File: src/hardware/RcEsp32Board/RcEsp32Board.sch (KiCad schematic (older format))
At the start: 2 parts

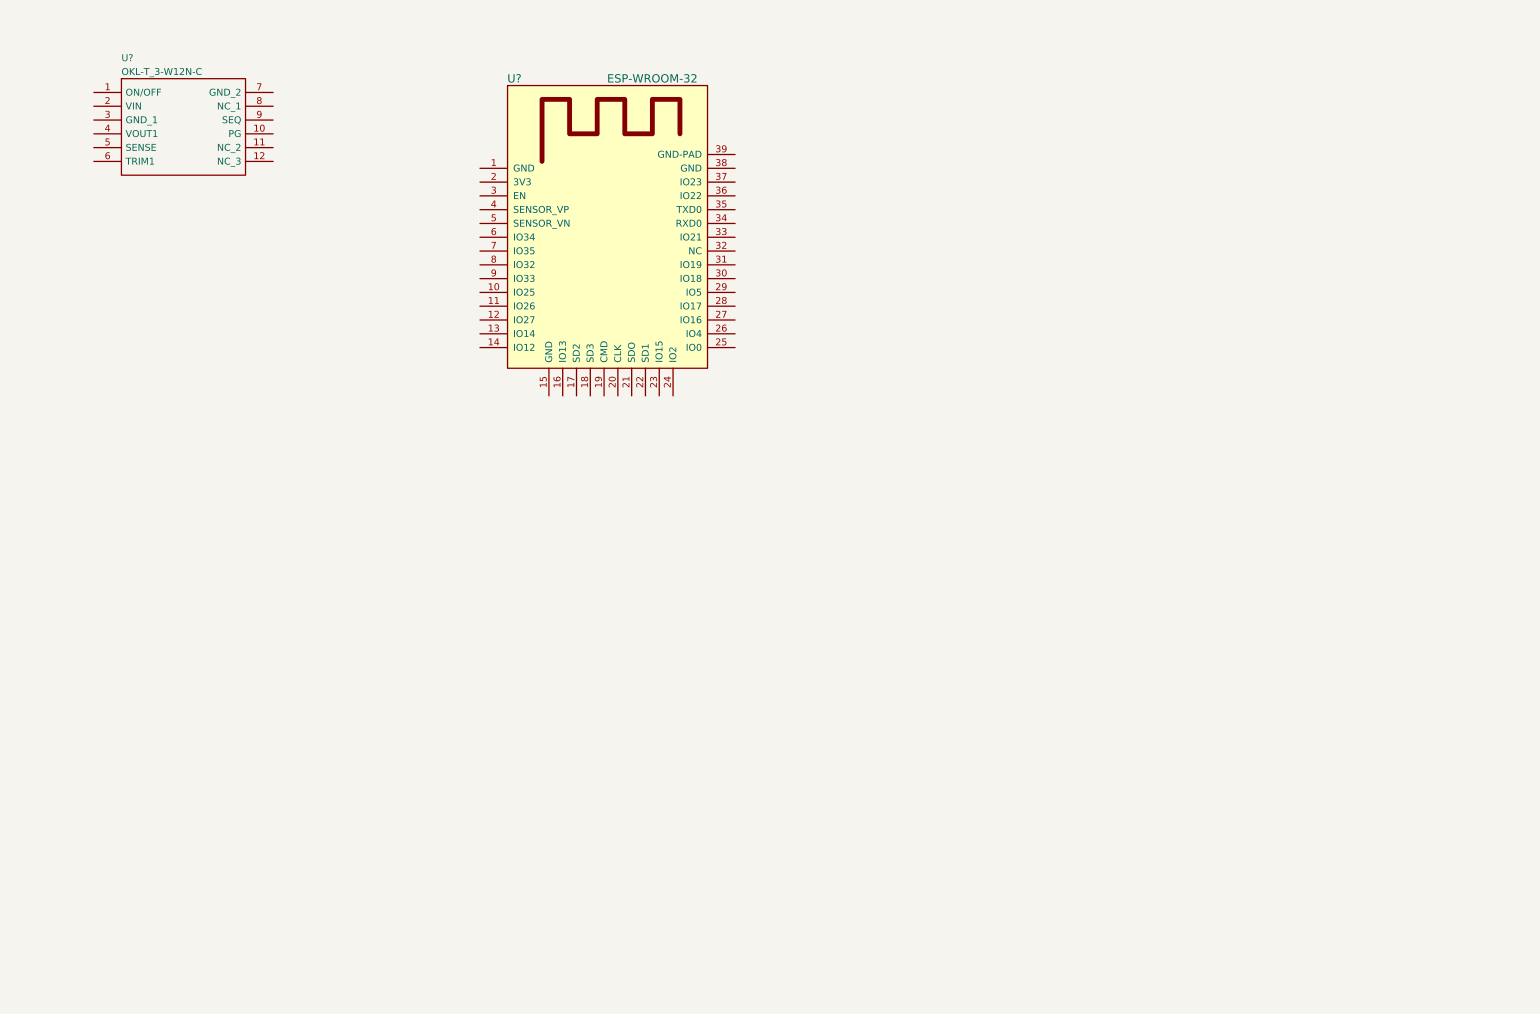
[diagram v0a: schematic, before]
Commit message: add components and update sch
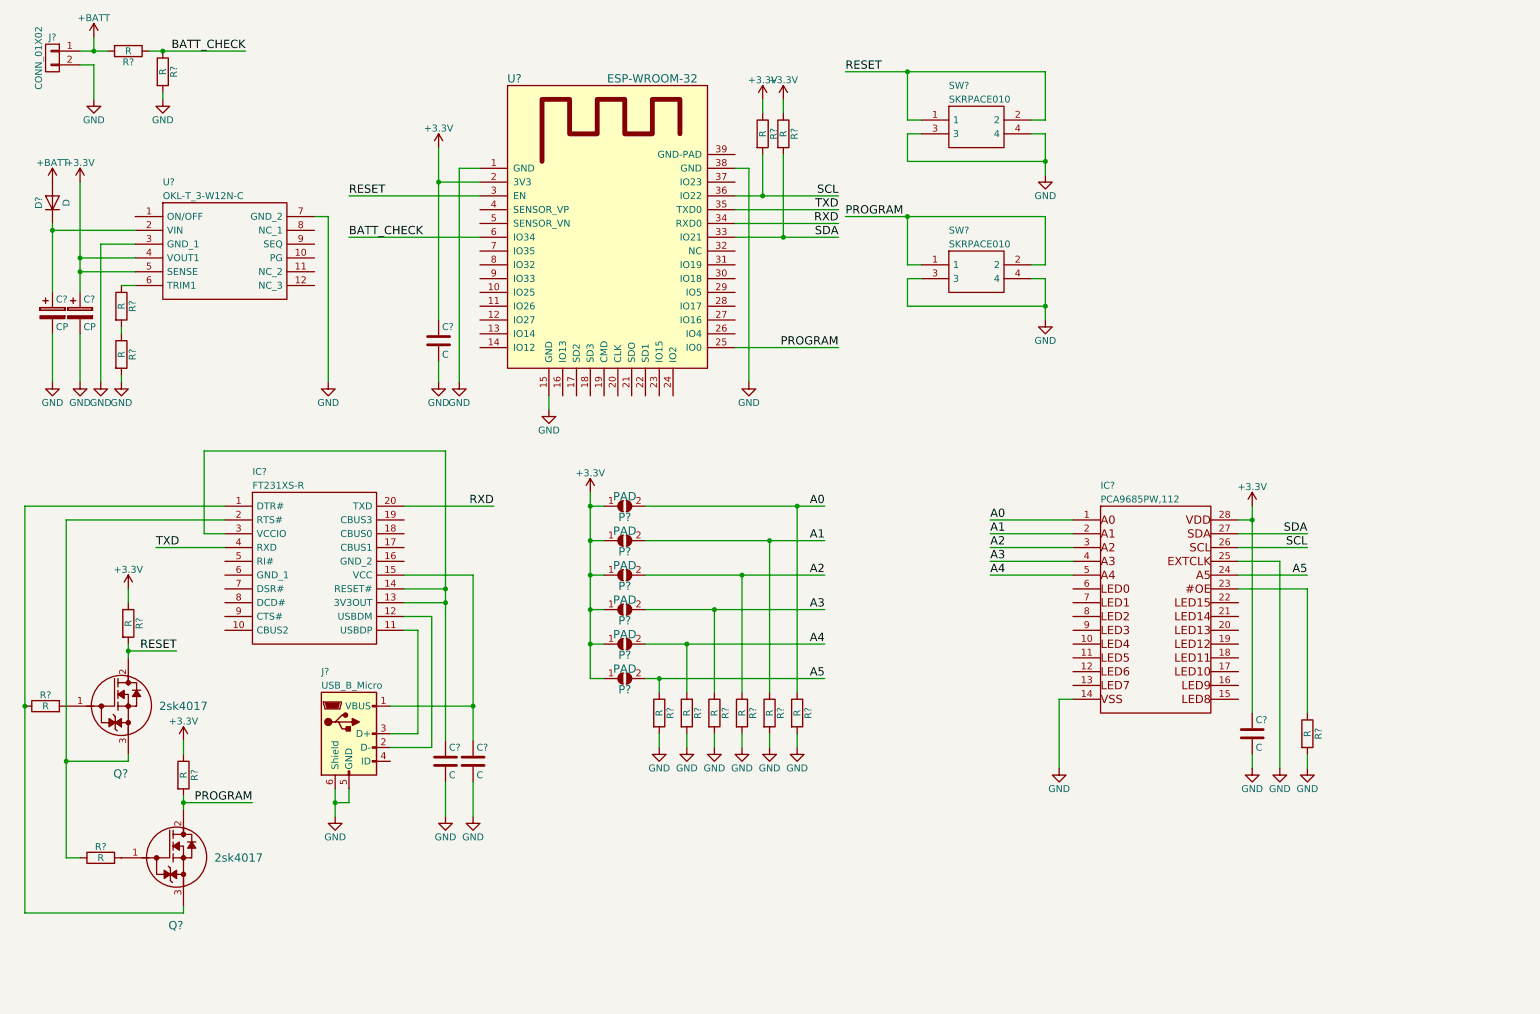
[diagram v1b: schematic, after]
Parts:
- added C? (x2): CP, symbol CP
- added C? (x4): C, symbol C
- added D?: D, symbol D
- added IC?: PCA9685PW,112, Elebot_footprint:SOP65P640X110-28N, symbol PCA9685PW,112
- added IC?: FT231XS-R, Elebot_footprint:SOP64P599X175-20N, symbol FT231XS-R
- added J?: CONN_01X02, Elebot_footprint:PinHeader01x02, symbol CONN_01X02
- added J?: USB_B_Micro, Elebot_footprint:USB_Micro-B_Molex-105133-0001, symbol USB_B_Micro
- added P? (x6): PAD, symbol PAD
- added Q? (x2): 2sk4017, symbol 2sk4017
- added R? (x17): R, symbol R
- added SW? (x2): SKRPACE010, Elebot_footprint:SMT(4.2X3.2), symbol SKRPACE010
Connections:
- net GND: now reaches U?.1 (GND)
- net GND: now also U?.15 (GND), U?.3 (GND_1), U?.38 (GND), U?.7 (GND_2), C?.2, C?.2, C?.2, C?.2, C?.2, C?.2, IC?.14, IC?.25, J?.2 (P2), J?.5 (GND), J?.6 (Shield), R?.2, R?.2, R?.2, R?.2, R?.2, R?.2, R?.2, R?.2, R?.2, SW?.3, SW?.3, SW?.4, SW?.4
- net +3V3: now reaches U?.2 (3V3)
- net +3V3: now also U?.4 (VOUT1), U?.5 (SENSE), C?.1, C?.1, C?.1, IC?.28, P?.1, P?.1, P?.1, P?.1, P?.1, P?.1, R?.1, R?.1, R?.1, R?.1
- net PROGRAM: now reaches U?.25 (IO0)
- net PROGRAM: now also Q?.2, R?.2, SW?.1, SW?.2
- net RESET: now reaches U?.3 (EN)
- net RESET: now also Q?.2, R?.2, SW?.1, SW?.2
- net SDA: now reaches U?.33 (IO21)
- net SDA: now also IC?.27, R?.2
- net RXD: now reaches U?.34 (RXD0)
- net RXD: now also IC?.20 (TXD)
- net TXD: now reaches U?.35 (TXD0)
- net TXD: now also IC?.4 (RXD)
- net SCL: now reaches U?.36 (IO22)
- net SCL: now also IC?.26, R?.2
- net BATT_CHECK: now reaches U?.6 (IO34)
- net BATT_CHECK: now also R?.1, R?.1
- net at U?.2 (VIN): now also C?.1, D?.1 (K)
- net at U?.6 (TRIM1): now also R?.1
- new net: R?.1, R?.2
- new net: IC?.23, R?.1
- new net: IC?.1 (DTR#), Q?.3, R?.1
- new net: IC?.11 (USBDP), J?.3 (D+)
- new net: IC?.12 (USBDM), J?.2 (D-)
- new net: C?.1, IC?.13 (3V3OUT), IC?.14 (RESET#), IC?.3 (VCCIO)
- new net: C?.1, IC?.15 (VCC), J?.1 (VBUS)
- new net: IC?.2 (RTS#), Q?.3, R?.1
- new net: Q?.1, R?.2 (x2)
- new net +BATT: D?.2 (A), J?.1 (P1), R?.2
- new net A0: IC?.1, P?.2, R?.1
- new net A1: IC?.2, P?.2, R?.1
- new net A2: IC?.3, P?.2, R?.1
- new net A3: IC?.4, P?.2, R?.1
- new net A4: IC?.5, P?.2, R?.1
- new net A5: IC?.24, P?.2, R?.1
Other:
- moved on the sheet: U?

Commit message: update
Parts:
- removed C?: C, symbol C
- removed IC?: PCA9685PW,112, Elebot_footprint:SOP65P640X110-28N, symbol PCA9685PW,112
- removed J?: CONN_01X02, Elebot_footprint:PinHeader01x02, symbol CONN_01X02
- removed P? (x6): PAD, symbol PAD
- removed Q? (x2): 2sk4017, symbol 2sk4017
- removed R? (x12): R, symbol R
- added J1: Conn_01x02, FootPrints:EH-2P, symbol Conn_01x02
- added J10, J3, J6, J8: Conn_01x04, FootPrints:PinHeader01x04, symbol Conn_01x04
- added J4, J7, J9: Conn_02x04_Odd_Even, FootPrints:PinHeader02x04, symbol Conn_02x04_Odd_Even
- added J5: Conn_01x03, FootPrints:PinHeader01x03, symbol Conn_01x03
- added LD2: LED, FootPrints:LED_1206_HandSoldering, symbol LED
- added P1, P2: PAD, FootPrints:PAD, symbol PAD
- added R5: 150, FootPrints:R_1206_HandSoldering, symbol R
- added R7, R8: R, FootPrints:R_1206_HandSoldering, symbol R
- C1, C2: renamed from C?; footprint (none) -> FootPrints:elecon_8x10_5
- C3, C4, C5: renamed from C?; value C -> 0.1u; footprint (none) -> FootPrints:C_1206_HandSoldering
- D1: renamed from D?; footprint (none) -> FootPrints:D_SOD-323_HandSoldering
- IC2: renamed from IC?; footprint Elebot_footprint:SOP64P599X175-20N -> FootPrints:SOP64P599X175-20N
- J2: renamed from J?; footprint Elebot_footprint:USB_Micro-B_Molex-105133-0001 -> FootPrints:USB_Micro-B_Molex-105133-0001
- R1: renamed from R?; value R -> 20K; footprint (none) -> FootPrints:R_1206_HandSoldering
- R2, R6: renamed from R?; value R -> 10K; footprint (none) -> FootPrints:R_1206_HandSoldering
- R3: renamed from R?; value R -> 1.5K; footprint (none) -> FootPrints:R_1206_HandSoldering
- R4: renamed from R?; value R -> 680; footprint (none) -> FootPrints:R_1206_HandSoldering
- SW1, SW2: renamed from SW?; footprint Elebot_footprint:SMT(4.2X3.2) -> FootPrints:SMT(4.2X3.2)
- U1: renamed from U?; footprint Elebot_footprint:OKL-T3-W12 -> FootPrints:OKL-T3-W12
- U2: renamed from U?; footprint ESP-WROOM-32 -> FootPrints:ESP-WROOM-32
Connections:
- net +3V3: now also J10.2 (Pin_2), J5.3 (Pin_3), J9.1 (Pin_1), J9.3 (Pin_3), J9.5 (Pin_5), J9.7 (Pin_7), R5.2, R7.1, R8.1
- net +BATT: now also J1.1 (Pin_1), J4.1 (Pin_1), J4.3 (Pin_3), J4.5 (Pin_5), J4.7 (Pin_7), J5.1 (Pin_1)
- net GND: now also U1.1 (ON/OFF), U2.39 (GND-PAD), J1.2 (Pin_2), J10.1 (Pin_1), J4.2 (Pin_2), J4.4 (Pin_4), J4.6 (Pin_6), J4.8 (Pin_8), J7.2 (Pin_2), J7.4 (Pin_4), J7.6 (Pin_6), J7.8 (Pin_8), J9.2 (Pin_2), J9.4 (Pin_4), J9.6 (Pin_6), J9.8 (Pin_8), LD2.1 (K)
- net SCL: now also J10.4 (Pin_4), P1.2
- net SDA: now also J10.3 (Pin_3), P2.2
- net IO0: now reaches U2.10 (IO25)
- net IO0: now also J6.1 (Pin_1)
- net IO1: now reaches U2.11 (IO26)
- net IO1: now also J6.2 (Pin_2)
- net IO2: now reaches U2.12 (IO27)
- net IO2: now also J6.3 (Pin_3)
- net IO3: now reaches U2.13 (IO14)
- net IO3: now also J6.4 (Pin_4)
- net INPUT3: now reaches U2.14 (IO12)
- net INPUT3: now also J8.4 (Pin_4)
- net SVR3: now reaches U2.26 (IO4)
- net SVR3: now also J3.4 (Pin_4)
- net SVR2: now reaches U2.27 (IO16)
- net SVR2: now also J3.3 (Pin_3)
- net SVR1: now reaches U2.28 (IO17)
- net SVR1: now also J3.2 (Pin_2)
- net SVR0: now reaches U2.29 (IO5)
- net SVR0: now also J3.1 (Pin_1)
- net INPUT0: now reaches U2.7 (IO35)
- net INPUT0: now also J8.1 (Pin_1)
- net INPUT1: now reaches U2.8 (IO32)
- net INPUT1: now also J8.2 (Pin_2)
- net INPUT2: now reaches U2.9 (IO33)
- net INPUT2: now also J8.3 (Pin_3)
- new net: LD2.2 (A), R5.1
- new net: J5.2 (Pin_2), J7.1 (Pin_1), J7.3 (Pin_3), J7.5 (Pin_5), J7.7 (Pin_7)
- new net: P2.1, R8.2
- new net: P1.1, R7.2
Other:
- note added: "CPU"
- note added: "I2C"
- note added: "INPUT(Analog/Digital)"
- note added: "IO(selectable power)"
- note added: "POWER"
- note added: "POWER LED"
- note added: "SERVO OUT"
- note added: "SWITCH"
- note added: "USB Serial"
- moved on the sheet: C1, C2, C3, C4, C5, D1, IC2, J2, R1, R2, R3, R4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

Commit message: update sch/pcb, add gerber data.
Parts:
- renumbered LD2 to LD1
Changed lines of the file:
@@
 EESchema Schematic File Version 2
-LIBS:RcEsp32Board-rescue
 LIBS:power
 LIBS:device
@@
 LIBS:valves
 LIBS:RcEsp32Components
-LIBS:Connector_Generic
 LIBS:RcEsp32Board-cache
 EELAYER 25 0
@@
 $EndComp
 $Comp
-L LED LD2
+L LED LD1
 U 1 1 5C29E336
 P 4400 4350
-F 0 "LD2" H 4400 4450 50  0000 C CNN
+F 0 "LD1" H 4400 4450 50  0000 C CNN
 F 1 "LED" H 4400 4250 50  0000 C CNN
 F 2 "FootPrints:LED_1206_HandSoldering" H 4400 4350 50  0001 C CNN

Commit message: update
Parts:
- C1, C2: symbol CP -> Device:CP
- C3, C4, C5: symbol C -> Device:C
- D1: symbol D -> Device:D
- IC2: symbol FT231XS-R -> RcEsp32Components:FT231XS-R
- J1: symbol Conn_01x02 -> RcEsp32Components:Conn_01x02
- J10, J3, J6, J8: symbol Conn_01x04 -> RcEsp32Components:Conn_01x04
- J2: symbol USB_B_Micro -> RcEsp32Components:USB_B_Micro
- J4, J7, J9: symbol Conn_02x04_Odd_Even -> RcEsp32Components:Conn_02x04_Odd_Even
- J5: symbol Conn_01x03 -> RcEsp32Components:Conn_01x03
- LD1: symbol LED -> Device:LED
- P1, P2: symbol PAD -> RcEsp32Components:PAD
- R1, R2, R3, R4, R5, R6, R7, R8: symbol R -> Device:R
- SW1, SW2: symbol SKRPACE010 -> RcEsp32Components:SKRPACE010
- U1: symbol OKL-T_3-W12N-C -> RcEsp32Components:OKL-T_3-W12N-C
- U2: symbol ESP-WROOM-32 -> RcEsp32Components:ESP-WROOM-32
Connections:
- net GND: now also IC2.16 (GND_2), IC2.6 (GND_1)
- net INPUT3: now also U2.16 (IO13); no longer U2.14 (IO12)
